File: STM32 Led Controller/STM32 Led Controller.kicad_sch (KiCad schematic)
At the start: 21 parts, among them J1 USB_C_Receptacle_USB2.0_16P, SW1 SW_Push, U1 STM32G0B0RETx, U2 Mini360, U3 NCV1117ST33T3G, U4 DML3006LFDS-7, U5 SN74AHCT125N, Y2 ABM8-48.000MHZ-B2-T

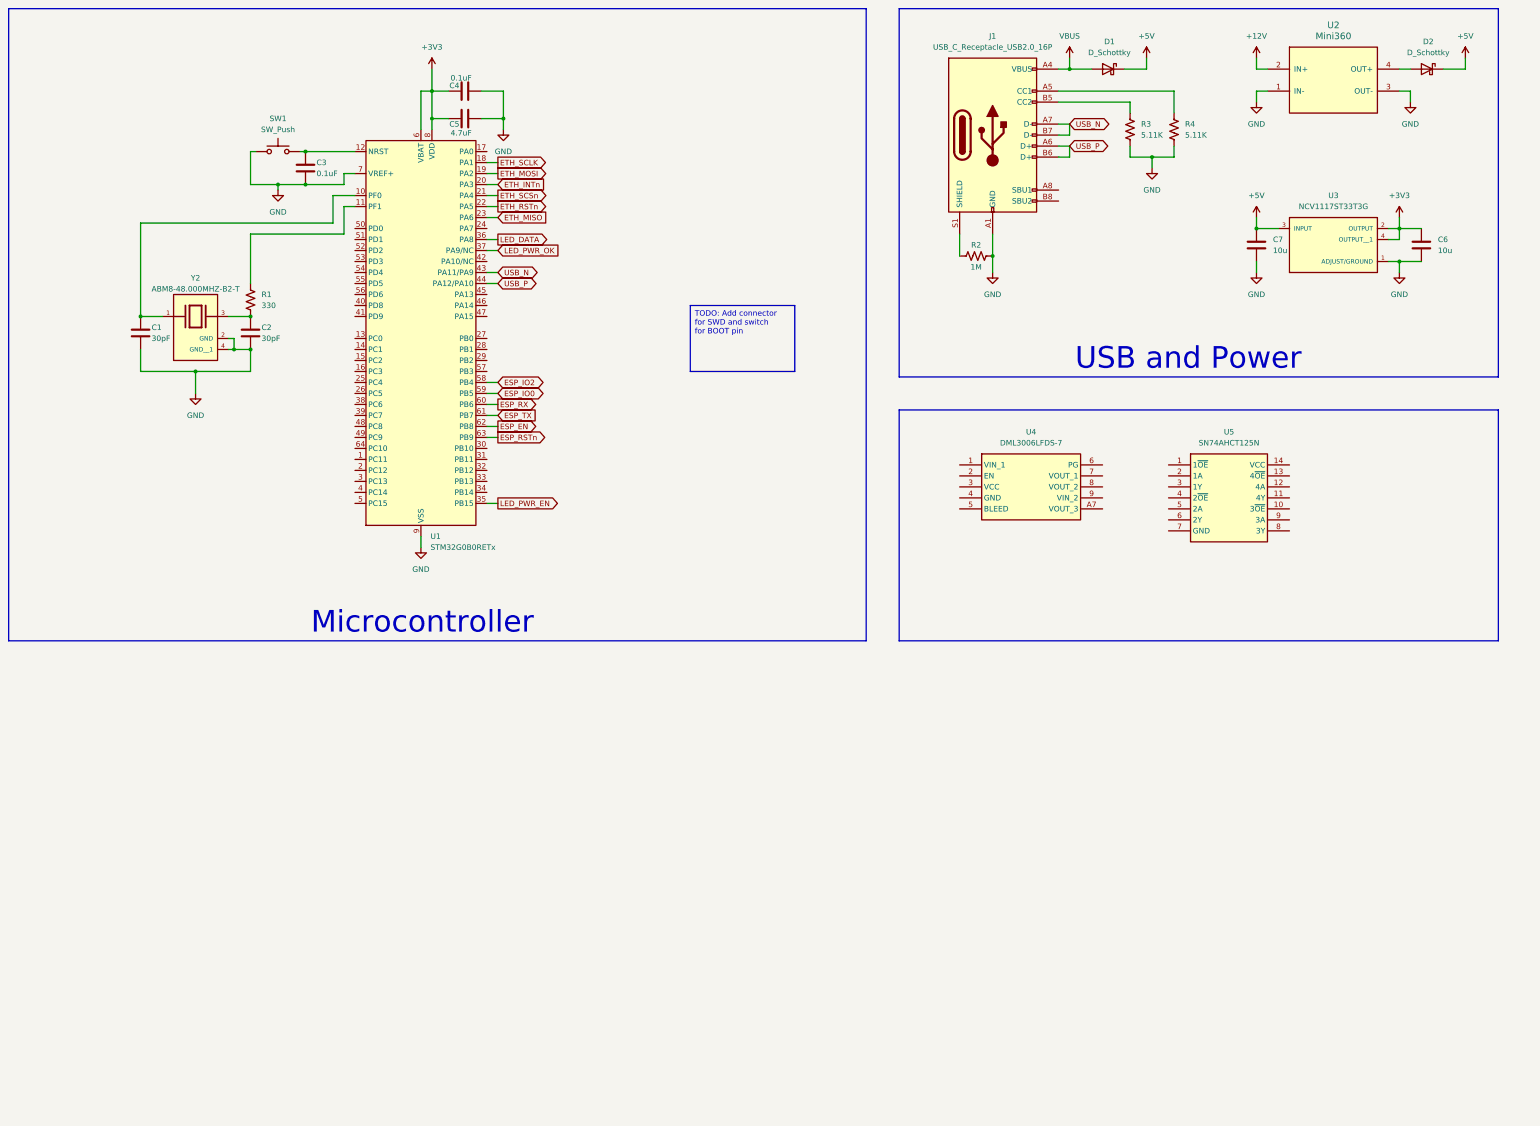
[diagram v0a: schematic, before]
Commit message: Tweaked schematic Initial PCB layout/wiring (subject to change) Still need to add name/rev to silk screen
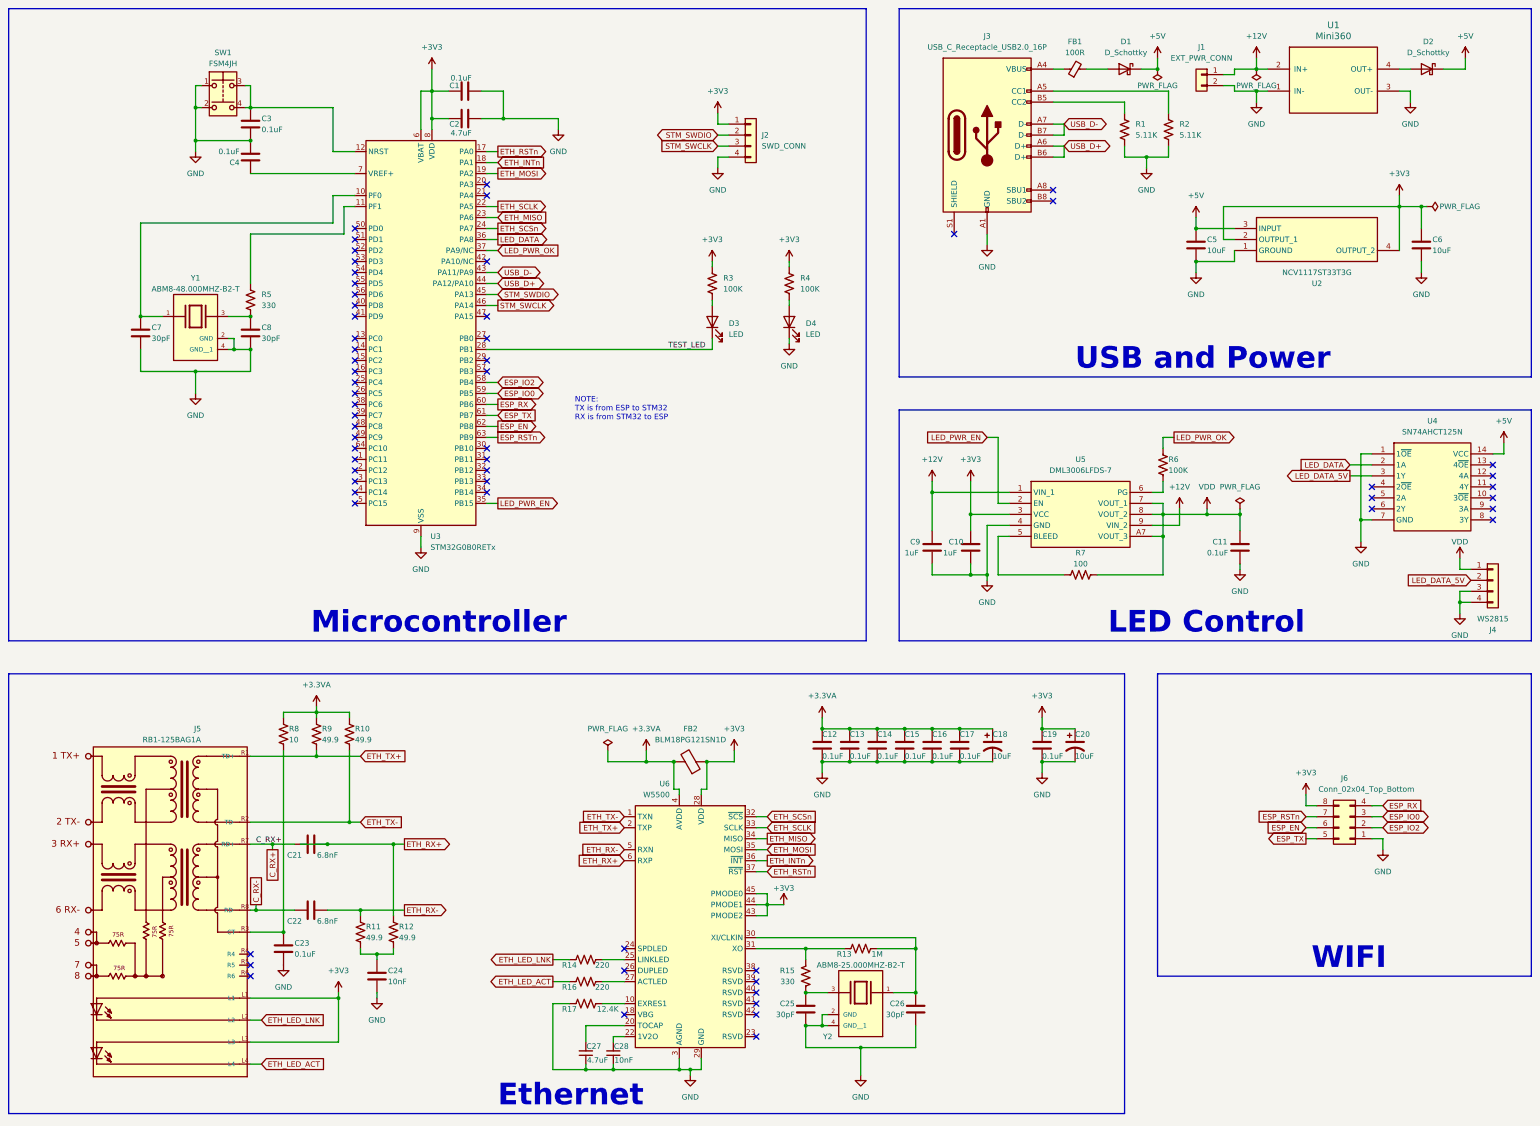
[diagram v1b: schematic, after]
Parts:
- removed R2: 1M, symbol Device:R_US
- removed SW1: SW_Push, symbol Switch:SW_Push
- removed U2: Mini360, Mini360_step-down:Mini360_step-down, symbol mini 360:Mini360
- removed U3: NCV1117ST33T3G, SnapEDA Library:SOT230P700X180-4N, symbol NCV1117ST33T3G:NCV1117ST33T3G
- added C10, C9: 1uF, Capacitor_SMD:C_0603_1608Metric, symbol Device:C
- added C11, C12, C13, C14, C15, C16, C17, C19, C23, C4: 0.1uF, Capacitor_SMD:C_0603_1608Metric, symbol Device:C
- added C18, C20: 10uF, Capacitor_SMD:CP_Elec_4x5.3, symbol Device:C_Polarized_US
- added C21, C22: 6.8nF, Capacitor_SMD:C_0603_1608Metric, symbol Device:C
- added C24: 10nF, Capacitor_SMD:C_0603_1608Metric, symbol Device:C
- added C25, C26: 30pF, Capacitor_SMD:C_0603_1608Metric, symbol Device:C
- added C27: 4.7uF, Capacitor_SMD:C_0603_1608Metric, symbol Device:C_Small
- added C28: 10nF, Capacitor_SMD:C_0603_1608Metric, symbol Device:C_Small
- added D3, D4: LED, LED_SMD:LED_0603_1608Metric, symbol Device:LED
- added FB1: 100R, Inductor_SMD:L_0805_2012Metric, symbol Device:FerriteBead_Small
- added FB2: BLM18PG121SN1D, SamacSys_Parts:BLM18SP221SN1B, symbol Device:FerriteBead
- added J1: EXT_PWR_CONN, Custom Connectors:1x02 M4 RING, symbol Connector_Generic:Conn_01x02
- added J2: SWD_CONN, Connector_PinHeader_2.54mm:PinHeader_1x04_P2.54mm_Vertical, symbol Connector_Generic:Conn_01x04
- added J4: WS2815, Custom Connectors:LED Strip Connector, symbol Connector_Generic:Conn_01x04
- added J5: RB1-125BAG1A, RB1-125BAG1A:WIZNET_RB1-125BAG1A, symbol RB1-125BAG1A:RB1-125BAG1A
- added J6: Conn_02x04_Top_Bottom, Connector_PinSocket_2.54mm:PinSocket_2x04_P2.54mm_Vertical, symbol Connector_Generic:Conn_02x04_Top_Bottom
- added R10, R11, R12, R9: 49.9, Resistor_SMD:R_0603_1608Metric, symbol Device:R_US
- added R13: 1M, Resistor_SMD:R_0603_1608Metric, symbol Device:R_US
- added R14, R16: 220, Resistor_SMD:R_0603_1608Metric, symbol Device:R_US
- added R15: 330, Resistor_SMD:R_0603_1608Metric, symbol Device:R_US
- added R17: 12.4K, Resistor_SMD:R_0603_1608Metric, symbol Device:R_US
- added R3, R4, R6: 100K, Resistor_SMD:R_0603_1608Metric, symbol Device:R_US
- added R7: 100, Resistor_SMD:R_0603_1608Metric, symbol Device:R_US
- added R8: 10, Resistor_SMD:R_0603_1608Metric, symbol Device:R_US
- added SW1: FSM4JH, SamacSys_Parts:FSM4JH, symbol Switch:SW_Push_Dual
- added U1: Mini360, Mini360_step-down:Mini360_step-down, symbol mini360:Mini360
- added U2: NCV1117ST33T3G, SamacSys_Parts:SOT230P700X180-4N, symbol SamacSys_Parts:NCV1117ST33T3G
- added U6: W5500, Package_QFP:LQFP-48_7x7mm_P0.5mm, symbol Interface_Ethernet:W5500
- added Y2: ABM8-25.000MHZ-B2-T, SnapEDA Library:XTAL_ABM8-48.000MHZ-B2-T, symbol ABM8-48.000MHZ-B2-T:ABM8-48.000MHZ-B2-T
- C1: renamed from C4; footprint (none) -> Capacitor_SMD:C_0603_1608Metric
- C2: renamed from C5; footprint (none) -> Capacitor_SMD:C_0603_1608Metric
- C3: footprint (none) -> Capacitor_SMD:C_0603_1608Metric
- C5: renamed from C7; value 10u -> 10uF; footprint (none) -> Capacitor_SMD:C_0805_2012Metric
- C6: value 10u -> 10uF; footprint (none) -> Capacitor_SMD:C_0805_2012Metric
- C7: renamed from C1; footprint (none) -> Capacitor_SMD:C_0603_1608Metric
- C8: renamed from C2; footprint (none) -> Capacitor_SMD:C_0603_1608Metric
- D1, D2: footprint (none) -> Diode_SMD:D_SMB-SMC_Universal_Handsoldering
- R1: renamed from R3; footprint (none) -> Resistor_SMD:R_0603_1608Metric
- R2: renamed from R4; footprint (none) -> Resistor_SMD:R_0603_1608Metric
- R5: renamed from R1; footprint (none) -> Resistor_SMD:R_0603_1608Metric
- renumbered J1 to J3, U1 to U3, U5 to U4, U4 to U5, Y2 to Y1
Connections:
- net +12V: now also U5.1 (VIN_1), U5.9 (VIN_2), C9.2, J1.1 (Pin_1), U1.2 (IN+)
- net +3V3: now also U5.3 (VCC), C10.2, C19.1, C20.1, FB2.1, J2.1 (Pin_1), J5.L1, J5.L3, J6.8 (Pin_8), R3.1, R4.1, U2.2 (OUTPUT_1), U2.4 (OUTPUT_2), U6.28 (VDD), U6.43 (PMODE2), U6.44 (PMODE1), U6.45 (PMODE0)
- net +5V: now also U4.14 (VCC), U2.3 (INPUT)
- net ESP_EN: now also J6.6 (Pin_6)
- net ESP_IO0: now also J6.3 (Pin_3)
- net ESP_IO2: now also J6.2 (Pin_2)
- net ESP_RSTn: now also J6.7 (Pin_7)
- net ESP_RX: now also J6.4 (Pin_4)
- net ESP_TX: now also J6.5 (Pin_5)
- net ETH_INTn: now also U3.18 (PA1), U6.36 (~{INT}); no longer U3.20 (PA3)
- net ETH_MISO: now also U6.34 (MISO)
- net ETH_MOSI: now also U6.35 (MOSI)
- net ETH_RSTn: now also U3.17 (PA0), U6.37 (~{RST}); no longer U3.22 (PA5)
- net ETH_SCLK: now also U3.22 (PA5), U6.33 (SCLK); no longer U3.18 (PA1)
- net ETH_SCSn: now also U3.24 (PA7), U6.32 (~{SCS}); no longer U3.21 (PA4)
- net GND: now also U4.1 (1~{OE}), U4.7 (GND), U5.4 (GND), C10.1, C11.1, C12.2, C13.2, C14.2, C15.2, C16.2, C17.2, C18.2, C19.2, C20.2, C23.2, C24.2, C25.2, C26.2, C27.1, C28.1, C4.2, C9.1, D4.1 (K), J1.2 (Pin_2), J2.4 (Pin_4), J4.3 (Pin_3), J4.4 (Pin_4), J6.1 (Pin_1), R17.2, SW1.1, SW1.2, U1.1 (IN-), U1.3 (OUT-), U2.1 (GROUND), U6.14 (AGND), U6.16 (AGND), U6.19 (AGND), U6.29 (GND), U6.3 (AGND), U6.48 (AGND), U6.9 (AGND), Y2.2 (GND), Y2.4 (GND__1); no longer U3.7 (VREF+)
- net LED_DATA: now also U4.2 (1A)
- net LED_PWR_EN: now also U5.2 (EN)
- net LED_PWR_OK: now also R6.2
- net at D2.2 (A): now also U1.4 (OUT+)
- net at U5.5 (BLEED): now also R7.1
- net at U5.6 (PG): now also R6.1
- net VDD: now reaches U5.7 (VOUT_1)
- net VDD: now also U5.8 (VOUT_2), U5.A7 (VOUT_3), C11.2, J4.1 (Pin_1), R7.2
- net at C3.1, U3.12 (NRST): now also SW1.3, SW1.4
- net TEST_LED: now reaches U3.28 (PB1)
- net TEST_LED: now also D3.1 (K)
- net STM_SWDIO: now reaches U3.45 (PA13)
- net STM_SWDIO: now also J2.2 (Pin_2)
- net STM_SWCLK: now reaches U3.46 (PA14)
- net STM_SWCLK: now also J2.3 (Pin_3)
- net LED_DATA_5V: now reaches U4.3 (1Y)
- net LED_DATA_5V: now also J4.2 (Pin_2)
- net USB_N renamed USB_D-
- net USB_P renamed USB_D+
- net VBUS: no longer names the net of J3.A4 (VBUS), J3.A9 (VBUS), J3.B4 (VBUS), J3.B9 (VBUS)
- net VBUS: now also FB1.1; no longer D1.2 (A)
- new net: R14.1, U6.25 (LINKLED)
- new net: C26.1, R13.1, U6.30 (XI/CLKIN), Y2.1
- new net: R13.2, R15.2, U6.31 (XO)
- new net: R16.1, U6.27 (ACTLED)
- new net: C25.1, R15.1, Y2.3
- new net: C4.1, U3.7 (VREF+)
- new net: C23.1, J5.R3 (CT), R8.2
- new net: C27.2, U6.20 (TOCAP)
- new net: C28.2, U6.22 (1V2O)
- new net: D1.2 (A), FB1.2
- new net: D3.2 (A), R3.2
- new net: C24.1, R11.2, R12.2
- new net: R17.1, U6.10 (EXRES1)
- new net: D4.2 (A), R4.2
- new net +3.3VA: C12.1, C13.1, C14.1, C15.1, C16.1, C17.1, C18.1, FB2.2, R10.1, R8.1, R9.1, U6.11 (AVDD), U6.15 (AVDD), U6.17 (AVDD), U6.21 (AVDD), U6.4 (AVDD), U6.8 (AVDD)
- new net C_RX+: C21.1, J5.R7 (RD+)
- new net C_RX-: C22.1, J5.R8 (RD-)
- new net ETH_LED_ACT: J5.L4, R16.2
- new net ETH_LED_LNK: J5.L2, R14.2
- new net ETH_RX+: C21.2, R12.1, U6.6 (RXP)
- new net ETH_RX-: C22.2, R11.1, U6.5 (RXN)
- new net ETH_TX+: J5.R1 (TD+), R9.2, U6.2 (TXP)
- new net ETH_TX-: J5.R2 (TD-), R10.2, U6.1 (TXN)
- no-connect marks 0 -> 61
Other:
- note added: "Ethernet"
- note added: "LED Control"
- note added: "NOTE: TX is from ESP to STM32 RX is from STM32 to ESP"
- note added: "WIFI"
- moved on the sheet: C3, C5, D1, J3, R1, R2, U4, U5
